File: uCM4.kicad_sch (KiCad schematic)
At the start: 80 parts, among them IC1 MAX17048G+, J1 Conn_02x07_Odd_Even, J10 USB_C_Receptacle, J11 SolderJumper_2_Open, J12 Conn_02x08_Odd_Even, J2 Micro_SD_Card_Det, J3 Conn_01x04, J4 Conn_01x04, J5 DummyJ, J6 DummyJ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

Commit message: Rearrangements
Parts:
- J1: footprint Connector_PinHeader_2.54mm:PinHeader_2x07_P2.54mm_Vertical -> Connector_PinHeader_2.54mm:PinHeader_2x07_P2.54mm_Vertical_SMD
- J3, J4: footprint Connector_JST:JST_PH_B4B-PH-K_1x04_P2.00mm_Vertical -> Connector_JST:JST_SH_BM03B-SRSS-TB_1x03-1MP_P1.00mm_Vertical
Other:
- note added: "Battery"
- note added: "Boost"
- note added: "Charger"
- note added: "Power path"
- note removed: "Bat + Boost"
- note removed: "Charging circuit"
- moved on the sheet: BT1, C11, C13, C4, C6, C7, C8, C9, D5, D6, D7, IC1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

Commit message: Changed some parts and hopeful final PCB arrangement.
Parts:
- removed D4: LED, symbol Device:LED
- removed D5: D, symbol Device:D
- removed J1: Conn_02x07_Odd_Even, Connector_PinHeader_2.54mm:PinHeader_2x07_P2.54mm_Vertical_SMD, symbol Connector_Generic:Conn_02x07_Odd_Even
- removed J3: Conn_01x04, Connector_JST:JST_SH_BM03B-SRSS-TB_1x03-1MP_P1.00mm_Vertical, symbol Connector_Generic:Conn_01x04
- removed Q1: PMOS, symbol Simulation_SPICE:PMOS
- removed R11, R5: 0, Resistor_SMD:R_0603_1608Metric_Pad0.98x0.95mm_HandSolder, symbol Device:R
- removed SW4: SW_Push, KiCAD_Randoms:PTS840_PM_SMTR_LFS, symbol Switch:SW_Push
- added D8: SS34, Diode_SMD:D_SMA, symbol Diode:SS34
- added J13: Conn_02x07_Odd_Even, Connector_PinHeader_2.54mm:PinHeader_2x07_P2.54mm_Vertical_SMD, symbol Connector_Generic:Conn_02x07_Odd_Even
- added Q2: AO3401A, Package_TO_SOT_SMD:SOT-23, symbol Transistor_FET:AO3401A
- added TP11, TP12: TestPoint, TestPoint:TestPoint_Pad_D1.0mm, symbol Connector:TestPoint
- BT1: footprint Connector_JST:JST_PH_S2B-PH-K_1x02_P2.00mm_Horizontal -> CM4:JST_B2B-PH-SM4-TB
- D3, D6, D7: footprint (none) -> LED_SMD:LED_0402_1005Metric
- J10: footprint Connector_USB:USB_C_Receptacle_Amphenol_12401610E4-2A -> Connector_USB:USB_C_Receptacle_GCT_USB4105-xx-A_16P_TopMnt_Horizontal
- J4: footprint Connector_JST:JST_SH_BM03B-SRSS-TB_1x03-1MP_P1.00mm_Vertical -> Connector_JST:JST_SH_BM04B-SRSS-TB_1x04-1MP_P1.00mm_Vertical
- R10: value 0 -> 1k; LCSC# C21189 -> C21190
- R21, R22, R24: footprint (none) -> Resistor_SMD:R_0402_1005Metric
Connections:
- net BAT_IN is gone; now on net BAT: TP10.1
- net +3V3: now also D3.2 (A), J12.4 (Pin_4)
- net +5V: now also J12.2 (Pin_2), J13.2 (Pin_2); no longer R10.2
- net BAT: now also Q2.3 (D)
- net BOOST_IN: now also D8.1 (K), Q2.2 (S), TP11.1
- net CTS0: now also J12.11 (Pin_11); no longer J12.3 (Pin_3)
- net GND: now also J12.6 (Pin_6), J13.1 (Pin_1)
- net RTS0: now also J12.3 (Pin_3); no longer J12.11 (Pin_11)
- net RXD0: now also J12.7 (Pin_7); no longer J12.9 (Pin_9)
- net RXD3: now also J13.3 (Pin_3)
- net RXD4: now also J13.13 (Pin_13)
- net SCL0: now also J13.10 (Pin_10)
- net SDA0: now also J13.9 (Pin_9)
- net TXD0: now also J12.9 (Pin_9); no longer J12.7 (Pin_7)
- net TXD3: now also J13.4 (Pin_4)
- net TXD4: now also J13.11 (Pin_11)
- net VBUS: now also D8.2 (A), Q2.1 (G), TP12.1
- net GPS_EXTINT: now reaches Module1.24 (GPIO26)
- net GPS_EXTINT: now also J13.8 (Pin_8)
- net SPI6_SCLK: now reaches Module1.25 (GPIO21)
- net SPI6_SCLK: now also J12.8 (Pin_8)
- net SPI6_MISO: now reaches Module1.26 (GPIO19)
- net SPI6_MISO: now also J12.10 (Pin_10)
- net SPI6_MOSI: now reaches Module1.27 (GPIO20)
- net SPI6_MOSI: now also J12.12 (Pin_12)
- net GPS_TIME_1: now reaches Module1.30 (GPIO6)
- net GPS_TIME_1: now also J13.5 (Pin_5)
- net GPS_TIME_2: now reaches Module1.38 (GPIO11)
- net GPS_TIME_2: now also J13.6 (Pin_6)
- net GPS_READY: now reaches Module1.44 (GPIO10)
- net GPS_READY: now also J13.7 (Pin_7)
- net GPIO22: now reaches Module1.46 (GPIO22)
- net GPIO22: now also R10.1
- net SPI6_CE1_N: now reaches Module1.48 (GPIO27)
- net SPI6_CE1_N: now also J12.16 (Pin_16)
- net SPI6_CE0_N: now reaches Module1.49 (GPIO18)
- net SPI6_CE0_N: now also J12.14 (Pin_14)
- net at D3.1 (K): now also R10.2
- net BTN1: no longer names the net of Module1.47 (GPIO23)
- no-connect marks 108 -> 101
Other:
- note added: "Check pinout"
- note added: "Does this switch make sense?"
- note added: "Make sure GPIOS work here"
- note added: "Remove all parts from bottom of board Check HaLow compat if possible"
- note removed: "AO3401A?"
- note removed: "Add SPI here"
- note removed: "Can def add/change this, have not altered"
- note removed: "Handle VBUS input to power path"
- note removed: "SPI output Remove all parts from bottom of board Check HaLow compat if possible"
- note removed: "This needs to be changed now"
- note removed: "USER LEDS"
- note removed: "Verify footprint match + choose pins"
- moved on the sheet: D3, R3

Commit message: Changed resistors to 0402
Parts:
- D1, D2: footprint LED_SMD:LED_0603_1608Metric_Pad1.05x0.95mm_HandSolder -> LED_SMD:LED_0402_1005Metric
- R10, R13, R15, R2, R20, R23, R3, R4: footprint Resistor_SMD:R_0603_1608Metric_Pad0.98x0.95mm_HandSolder -> Resistor_SMD:R_0402_1005Metric
- R12, R14, R16, R19: footprint Resistor_SMD:R_0603_1608Metric -> Resistor_SMD:R_0402_1005Metric
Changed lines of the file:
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@@
 			)
 		)
-		(property "Footprint" "Resistor_SMD:R_0603_1608Metric_Pad0.98x0.95mm_HandSolder"
+		(property "Footprint" "Resistor_SMD:R_0402_1005Metric"
 			(at 60.96 314.198 90)
 			(effects
@@
 			)
 		)
-		(property "Footprint" "Resistor_SMD:R_0603_1608Metric_Pad0.98x0.95mm_HandSolder"
+		(property "Footprint" "Resistor_SMD:R_0402_1005Metric"
 			(at 187.96 118.618 90)
 			(effects
@@
 			)
 		)
-		(property "Footprint" "LED_SMD:LED_0603_1608Metric_Pad1.05x0.95mm_HandSolder"
+		(property "Footprint" "LED_SMD:LED_0402_1005Metric"
 			(at 176.53 147.32 0)
 			(effects
@@
 			)
 		)
-		(property "Footprint" "Resistor_SMD:R_0603_1608Metric_Pad0.98x0.95mm_HandSolder"
+		(property "Footprint" "Resistor_SMD:R_0402_1005Metric"
 			(at 88.9 71.628 90)
 			(effects
@@
 			)
 		)
-		(property "Footprint" "Resistor_SMD:R_0603_1608Metric_Pad0.98x0.95mm_HandSolder"
+		(property "Footprint" "Resistor_SMD:R_0402_1005Metric"
 			(at 34.29 57.658 90)
 			(effects
@@
 			)
 		)
-		(property "Footprint" "Resistor_SMD:R_0603_1608Metric_Pad0.98x0.95mm_HandSolder"
+		(property "Footprint" "Resistor_SMD:R_0402_1005Metric"
 			(at 60.96 311.658 90)
 			(effects
@@
 			)
 		)
-		(property "Footprint" "Resistor_SMD:R_0603_1608Metric"
+		(property "Footprint" "Resistor_SMD:R_0402_1005Metric"
 			(at 341.63 60.198 90)
 			(effects
@@
 			)
 		)
-		(property "Footprint" "Resistor_SMD:R_0603_1608Metric"
+		(property "Footprint" "Resistor_SMD:R_0402_1005Metric"
 			(at 387.858 154.94 90)
 			(effects
@@
 			)
 		)
-		(property "Footprint" "Resistor_SMD:R_0603_1608Metric_Pad0.98x0.95mm_HandSolder"
+		(property "Footprint" "Resistor_SMD:R_0402_1005Metric"
 			(at 65.278 237.49 90)
 			(effects
@@
 			)
 		)
-		(property "Footprint" "Resistor_SMD:R_0603_1608Metric_Pad0.98x0.95mm_HandSolder"
+		(property "Footprint" "Resistor_SMD:R_0402_1005Metric"
 			(at 165.1 149.098 90)
 			(effects
@@
 			)
 		)
-		(property "Footprint" "LED_SMD:LED_0603_1608Metric_Pad1.05x0.95mm_HandSolder"
+		(property "Footprint" "LED_SMD:LED_0402_1005Metric"
 			(at 166.37 162.56 0)
 			(effects
@@
 			)
 		)
-		(property "Footprint" "Resistor_SMD:R_0603_1608Metric_Pad0.98x0.95mm_HandSolder"
+		(property "Footprint" "Resistor_SMD:R_0402_1005Metric"
 			(at 154.94 164.338 90)
 			(effects
@@
 			)
 		)
-		(property "Footprint" "Resistor_SMD:R_0603_1608Metric"
+		(property "Footprint" "Resistor_SMD:R_0402_1005Metric"
 			(at 393.7 152.908 90)
 			(effects
@@
 			)
 		)
-		(property "Footprint" "Resistor_SMD:R_0603_1608Metric"
+		(property "Footprint" "Resistor_SMD:R_0402_1005Metric"
 			(at 341.63 50.038 90)
 			(effects

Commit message: Changed capacitor sizes
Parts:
- C1, C11, C13, C2, C3: footprint Capacitor_SMD:C_0603_1608Metric -> Capacitor_SMD:C_0402_1005Metric
- C5: footprint Capacitor_SMD:C_0805_2012Metric -> Capacitor_SMD:C_0603_1608Metric
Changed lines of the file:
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@@
 			)
 		)
-		(property "Footprint" "Capacitor_SMD:C_0805_2012Metric"
+		(property "Footprint" "Capacitor_SMD:C_0603_1608Metric"
 			(at 230.8352 55.88 0)
 			(effects
@@
 			)
 		)
-		(property "Footprint" "Capacitor_SMD:C_0603_1608Metric"
+		(property "Footprint" "Capacitor_SMD:C_0402_1005Metric"
 			(at 452.12 123.4948 0)
 			(effects
@@
 			)
 		)
-		(property "Footprint" "Capacitor_SMD:C_0603_1608Metric"
+		(property "Footprint" "Capacitor_SMD:C_0402_1005Metric"
 			(at 378.7648 73.66 0)
 			(effects
@@
 			)
 		)
-		(property "Footprint" "Capacitor_SMD:C_0603_1608Metric"
+		(property "Footprint" "Capacitor_SMD:C_0402_1005Metric"
 			(at 382.27 143.8148 0)
 			(effects
@@
 			)
 		)
-		(property "Footprint" "Capacitor_SMD:C_0603_1608Metric"
+		(property "Footprint" "Capacitor_SMD:C_0402_1005Metric"
 			(at 361.95 39.6748 0)
 			(effects
@@
 			)
 		)
-		(property "Footprint" "Capacitor_SMD:C_0603_1608Metric"
+		(property "Footprint" "Capacitor_SMD:C_0402_1005Metric"
 			(at 367.03 41.6052 0)
 			(effects

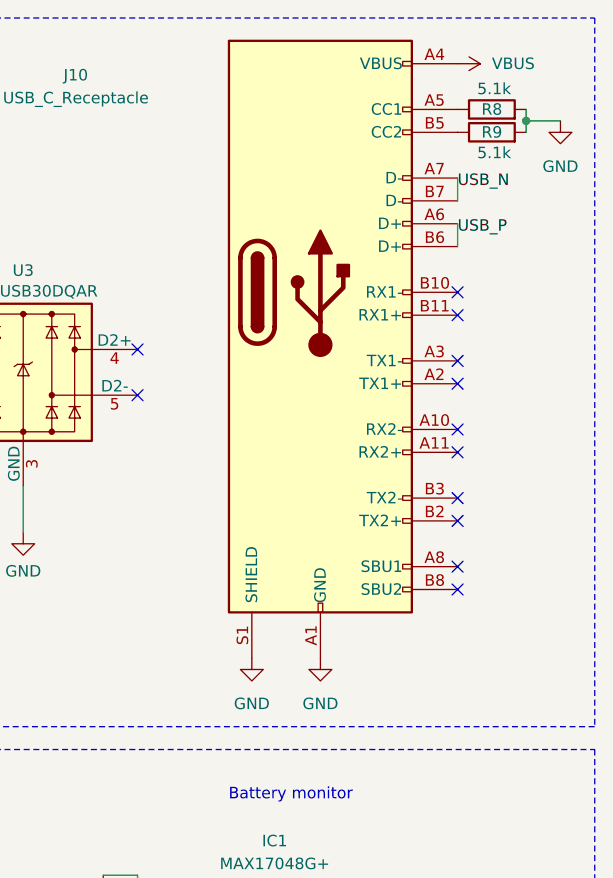
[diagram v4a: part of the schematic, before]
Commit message: Updated USB-C connector to be simpler.
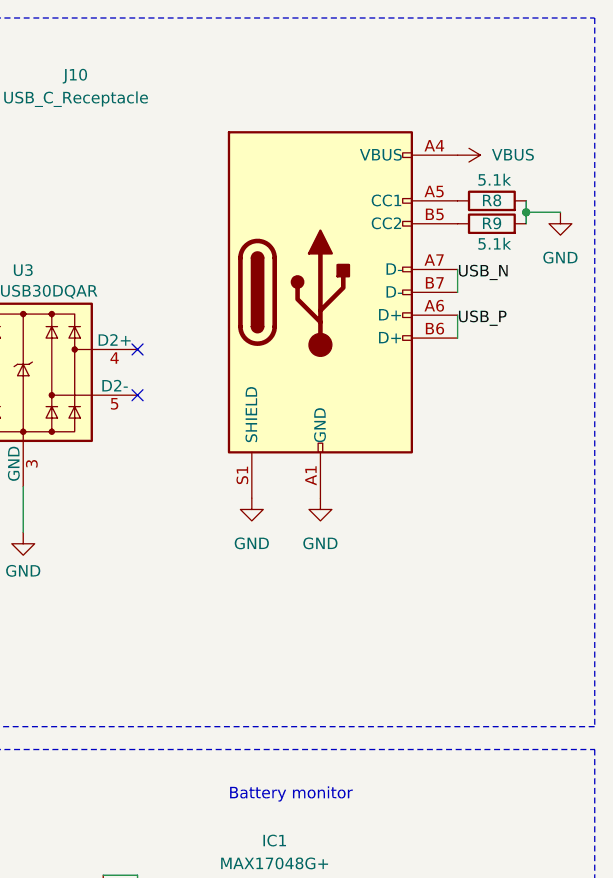
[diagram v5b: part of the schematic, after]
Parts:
- J10: symbol Connector:USB_C_Receptacle -> Connector:USB_C_Receptacle_USB2.0_14P
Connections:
- no-connect marks 101 -> 91
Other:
- moved on the sheet: R8, R9

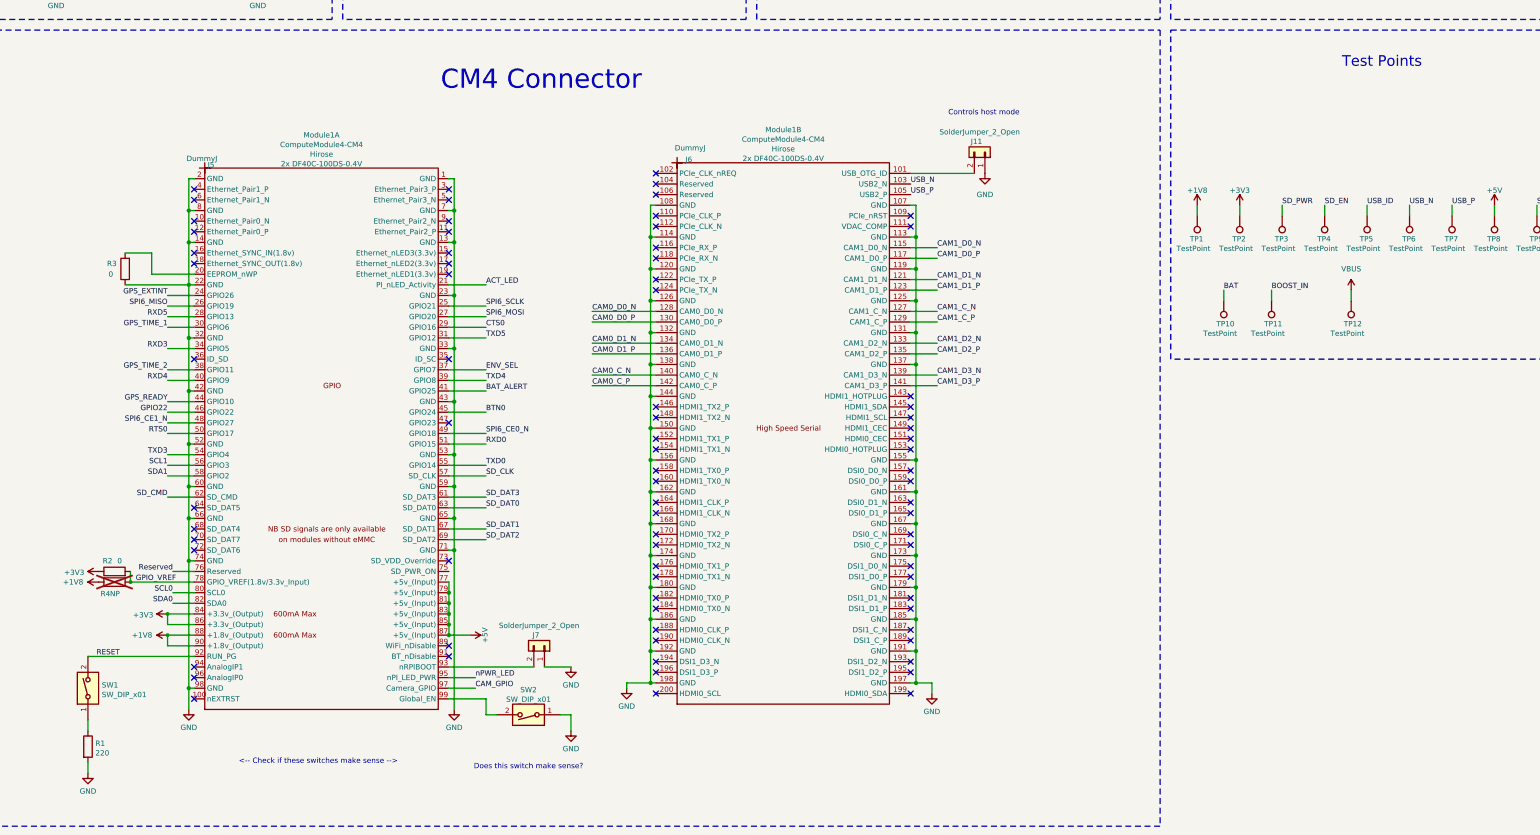
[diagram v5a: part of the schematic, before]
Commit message: Arranging and changing switches.
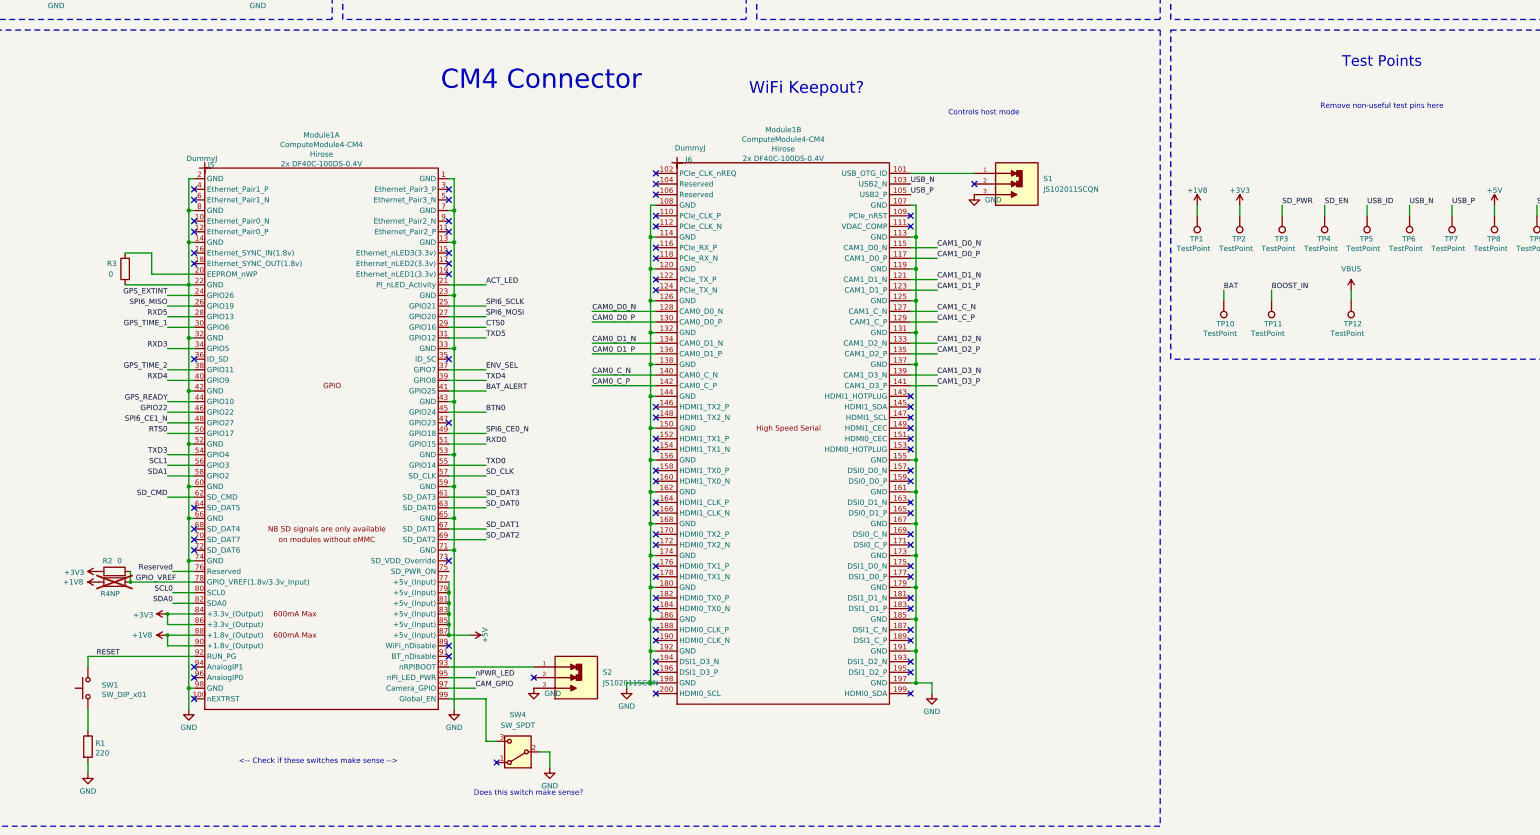
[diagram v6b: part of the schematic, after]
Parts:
- removed J11, J7: SolderJumper_2_Open, Connector_PinHeader_2.54mm:PinHeader_1x02_P2.54mm_Vertical_SMD_Pin1Left, symbol Connector_Generic:Conn_01x02
- removed SW2: SW_DIP_x01, KiCAD_Randoms:PTS840_PM_SMTR_LFS, symbol Switch:SW_DIP_x01
- added S1, S2: JS102011SCQN, CM4:SW_JS102011SCQN, symbol CM4IO:JS102011SCQN
- added SW4: SW_SPDT, Button_Switch_SMD:SW_SPDT_PCM12, symbol Switch:SW_SPDT
- SW1: symbol Switch:SW_DIP_x01 -> Switch:SW_Push
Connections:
- net GND: now also S1.3, S2.3, SW4.2 (B)
- net at Module1.101 (USB_OTG_ID): now also S1.1
- net at Module1.99 (Global_EN): now also SW4.3 (C)
- net at Module1.93 (nRPIBOOT): now also S2.1
- no-connect marks 91 -> 94
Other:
- note added: "Remove non-useful test pins here"
- note added: "WiFi Keepout?"

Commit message: Routing
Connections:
- net USB_P: now also U3.5 (D2-); no longer U3.2 (D1-)
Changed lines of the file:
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@@
 	)
 	(no_connect
-		(at 458.47 59.69)
-	)
-	(no_connect
 		(at 349.25 60.96)
 	)
@@
 	)
 	(no_connect
+		(at 433.07 59.69)
+	)
+	(no_connect
 		(at 80.01 259.08)
 	)
@@
 		)
 	)
-	(label "USB_P"
-		(at 433.07 59.69 180)
-		(effects
-			(font
-				(size 1.27 1.27)
-			)
-			(justify right bottom)
-		)
-	)
 	(label "USB_N"
 		(at 494.03 46.99 0)
@@
 		(effects
 			(font
+				(size 1.27 1.27)
+			)
+			(justify left bottom)
+		)
+	)
+	(label "USB_P"
+		(at 458.47 59.69 0)
+		(effects
+			(font

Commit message: Correcting symbols and routing progress.
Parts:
- BT1: symbol Device:Battery -> CM4IO:B2B-PH-SM4-TB; MANUFACTURER (none) -> JST; MAXIMUM_PACKAGE_HEIGHT (none) -> 6.6 mm; PARTREV (none) -> N/A; STANDARD (none) -> Manufacturer Recommendations
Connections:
- net GND: now also BT1.S1, BT1.S2, J4.MP, J8.MP, J9.MP
- no-connect marks 94 -> 97
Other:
- moved on the sheet: R23
